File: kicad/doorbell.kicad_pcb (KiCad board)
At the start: 4 copper layers, 64 x 59 mm, 76 parts, among them J1 USB-C (USB4105), J2 WF26 bus, K1 GAQW212GS, K2 GAQY212GS, K3 GAQY412EH, K4 GAQY412EH, K5 G6K-2F-Y DC12, Q3 2N7002DW-7-F, SW1 BOOT, SW2 EN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

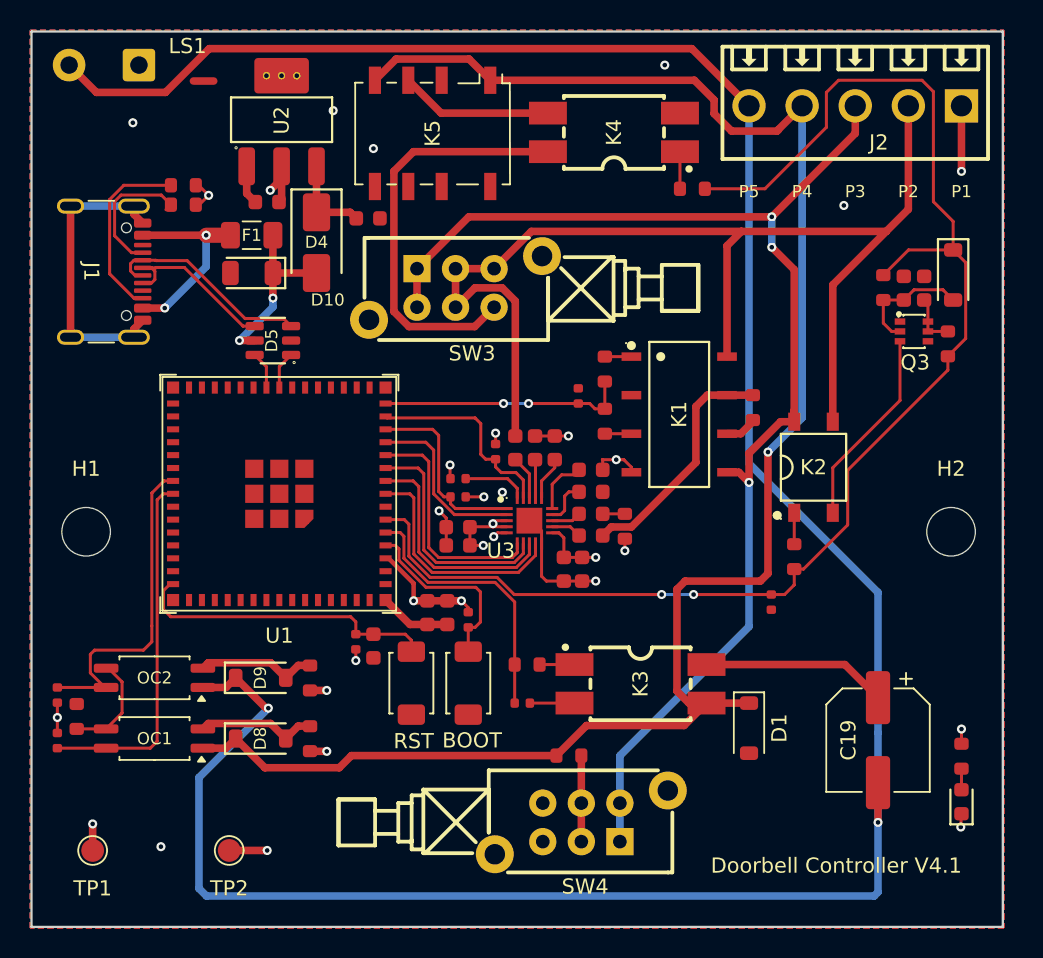
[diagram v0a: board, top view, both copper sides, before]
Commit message: PCB routing cleanup + K3 contact swap; confirm C1 polarity on the genuine WF26
Board (kicad/doorbell.*):
- P5 off the back layer: dropped the ~44 mm B.Cu bottom-edge run; OC2/D9 now tap
  P5 up the left edge to LS1, with C19 routed down the right edge. All-F.Cu, DRC clean.
- PTT_DRV all-F.Cu: removed the B.Cu hop under C16 (its via pair) by moving C16 up
  so PTT_DRV passes beneath it on the front; P2 now reaches C16 from the north, so
  the P2/PTT_DRV crossing that forced the hop is gone.
- Relocated the boot pull-downs to their MCU pins: R8 (DOOR_DRV) and R7 (PTT_DRV).
- K3 (chime mute): swapped the bidirectional PhotoMOS contact pins 3<->4
  (CHIME_C1 / P4) in the schematic for cleaner routing -- the output is symmetric.
- Zone refills; regenerated doorbell.pdf.

Docs:
- C1/C19 polarity bench-confirmed on the genuine WF26: + -> P4, - -> P5 (matches the
  wf26 reverse-engineered schematic and the V4 board; the old +->P5 assumption was the
  error). DESIGN.md + VERIFICATION.md updated, open item retired.
- reference/wf26.heic: genuine WF26 board photo (the polarity evidence).
- kicad/.gitignore: also ignore *_2d_view.png render artifacts.
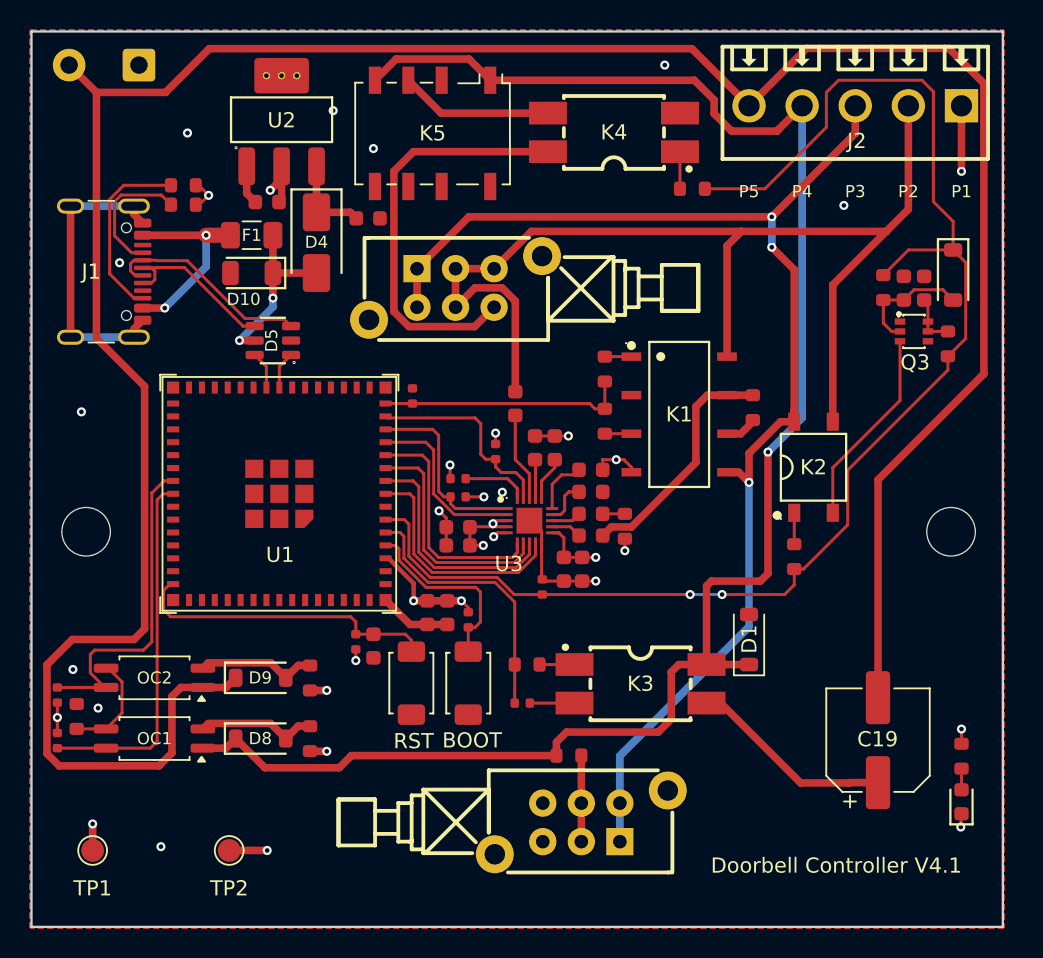
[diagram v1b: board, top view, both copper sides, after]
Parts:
- moved R8 15.1 mm to (50.1, 52.9), turned to 90 degrees
- moved R7 10.9 mm to (41.6, 40.3)
- moved D1 5.84 mm to (63.8, 56.4), turned to 90 degrees
- moved C16 2.92 mm to (48.4, 40.8)
- turned C19 to 90 degrees
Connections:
- K3 pad 3: /P4 -> /CHIME_C1
- K3 pad 4: /CHIME_C1 -> /P4
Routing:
- net /P5: track 169.8 -> 177.0 mm, vias 2 -> 0
- net /ES_MICP: track 2.91 -> 5.83 mm
- net /P2: track 77.2 -> 74.3 mm
- net /P4: track 118.0 -> 115.6 mm
- net GND: track 60.8 -> 59.4 mm, vias 20 -> 24
- net /CHIME_C1: track 12.2 -> 13.5 mm
- net /PTT_DRV: track 16.5 -> 16.4 mm, vias 2 -> 0

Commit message: Swap U1 to ESP32-C6-MINI-1U-H4: pinout, firmware, PCB re-layout
Replace the ESP32-S3-MINI-1U-N8 with the pin-compatible-in-spirit
ESP32-C6-MINI-1U-H4 (native USB-Serial-JTAG, u.FL external antenna,
4 MB flash) and carry the change through the whole stack.

- Schematic: U1 = ESP32-C6-MINI-1U-H4 with a new GPIO map (USB pads
  face north toward D5/J1, ES8311 I2S exits east in U3 pin order,
  I2C+MCLK off the NE corner). IO8 held high by R12 (SPI-boot strap,
  net IO8_STRAP); BOOT on IO9. U1 sourcing attrs set (LCSC C20627095,
  MPN, Value).
- Firmware: board esp32-c6-devkitc-1 / variant esp32c6 / flash 4MB;
  remap I2S/I2C/SSR-gate/opto-sense GPIOs to the C6 pinout.
  `esphome config` validates clean (only the expected GPIO4/GPIO5
  strapping-pin notices, which strap the unused SDIO boot edge).
- PCB: re-laid out for the C6 footprint and the new escape order.
- Docs: DESIGN.md MCU decision + GPIO-map rationale rewritten for the
  C6; VERIFICATION.md route-check note clarified.
- Component attrs: fill empty descriptions (J2, K1-K4, ...), replace
  library boilerplate with role descriptions, normalize resistor
  values (drop the inconsistent ohm suffix), fix R25 (6.8M one-shot).
- Tooling: build.sh gains a `sim` target; route.py float-sliver check
  now only fails islands actually wide enough to host a GND stitch via.
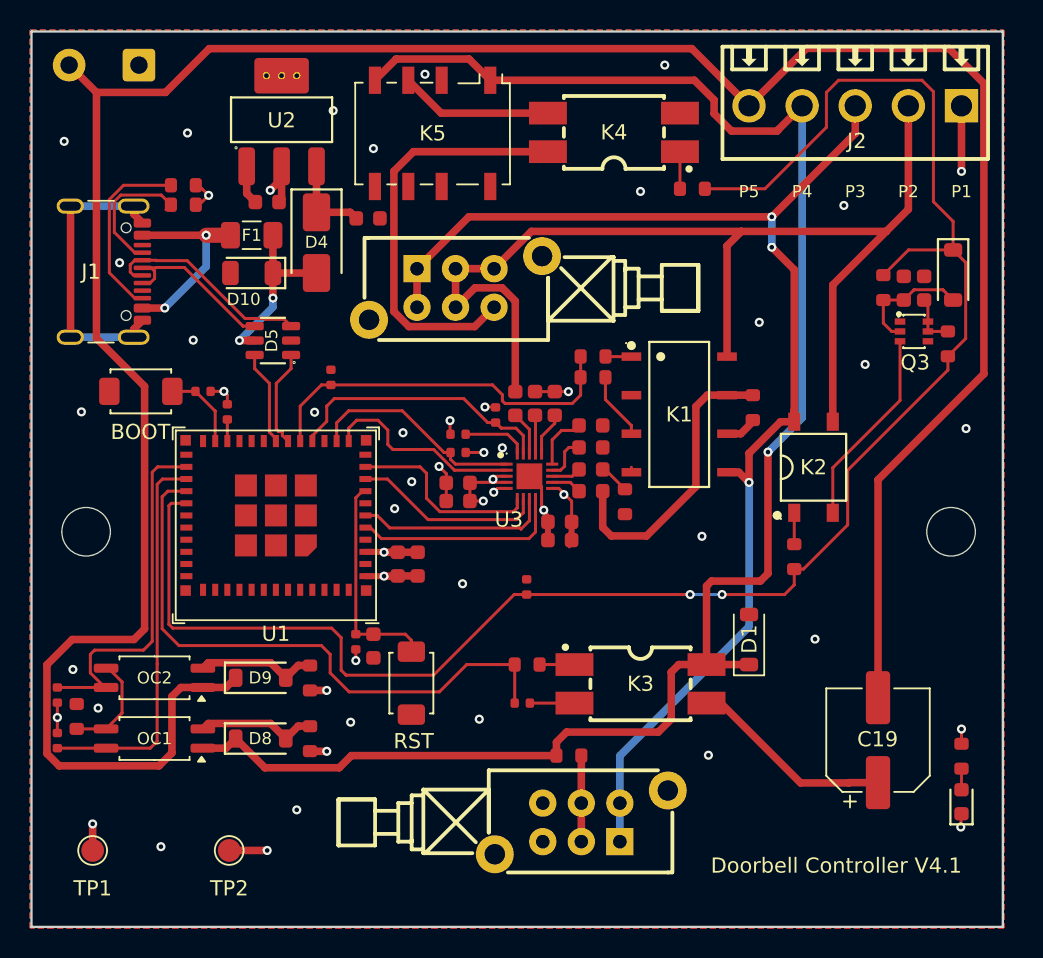
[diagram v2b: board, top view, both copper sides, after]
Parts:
- added R12: 10k, PCM_JLCPCB:R_0402, F.Cu at (29.4, 41.4)
- U1: value ESP32-S3-MINI-1U-N8 -> ESP32-C6-MINI-1U-H4; footprint PCM_Espressif:ESP32-S3-MINI-1U -> PCM_Espressif:ESP32-C6-MINI-1U
- moved SW1 28.9 mm to (23.7, 40.0), turned to 180 degrees
- moved R11 23.1 mm to (27.8, 40.0), turned to 180 degrees
- moved R7 5.51 mm to (36.2, 39.1)
- moved U1 4.13 mm to (32.6, 50.9)
- moved C3 3.75 mm to (41.9, 51.4)
- moved C6 3.75 mm to (40.6, 51.4)
- moved C9 3.13 mm to (51.3, 48.6), turned to 180 degrees
- moved R24 3.00 mm to (53.5, 39.1), turned to 180 degrees
- moved C11 2.93 mm to (53.3, 43.7)
- moved C12 2.93 mm to (51.0, 40.8)
- moved C13 2.93 mm to (53.3, 42.2)
- moved C14 2.93 mm to (53.3, 46.6)
- moved C17 2.93 mm to (49.6, 40.8)
- moved C7 2.93 mm to (44.6, 47.2)
- moved C8 2.93 mm to (44.6, 46.0)
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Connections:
- U1 pad 10: /I2S_DIN -> /I2S_BCLK
- U1 pad 11: /I2S_BCLK -> GND
- U1 pad 14: /I2C_SDA -> GND
- U1 pad 15: /PTT_DRV -> /I2C_SDA
- U1 pad 16: unconnected-(U1-IO12-Pad16) -> /PTT_DRV
- U1 pad 17: unconnected-(U1-IO13-Pad17) -> /USB_ESP_DN
- U1 pad 18: unconnected-(U1-IO14-Pad18) -> /USB_ESP_DP
- U1 pad 22: unconnected-(U1-IO18-Pad22) -> /IO8_STRAP
- U1 pad 23: /USB_ESP_DN -> /BOOT
- U1 pad 24: /USB_ESP_DP -> unconnected-(U1-GPIO18-Pad24)
- U1 pad 26: unconnected-(U1-IO26-Pad26) -> /OC2_OUT
- U1 pad 27: unconnected-(U1-IO47-Pad27) -> /OC1_OUT
- U1 pad 28: unconnected-(U1-IO33-Pad28) -> /MUTE_DRV
- U1 pad 29: unconnected-(U1-IO34-Pad29) -> /DOOR_DRV
- U1 pad 36: unconnected-(U1-IO40-Pad36) -> GND
- U1 pad 37: /OC2_OUT -> GND
- U1 pad 38: /OC1_OUT -> GND
- U1 pad 39: unconnected-(U1-TXD0-Pad39) -> GND
- U1 pad 4: /BOOT -> unconnected-(U1-NC-Pad4)
- U1 pad 40: unconnected-(U1-RXD0-Pad40) -> GND
- U1 pad 41: unconnected-(U1-IO45-Pad41) -> GND
- U1 pad 44: unconnected-(U1-IO46-Pad44) -> GND
- U1 pad 45: /EN -> GND
- U1 pad 5: /MUTE_DRV -> /I2S_DOUT
- U1 pad 6: /DOOR_DRV -> /I2S_WS
- U1 pad 8: /I2S_DOUT -> /EN
- U1 pad 9: /I2S_WS -> /I2S_DIN
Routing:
- net /DOOR_DRV: track 93.9 -> 118.7 mm
- net /MUTE_DRV: track 18.2 -> 39.6 mm
- net /PTT_DRV: track 16.4 -> 24.9 mm
- net GND: track 59.4 -> 51.0 mm, vias 24 -> 41
- net /BOOT: track 12.5 -> 5.34 mm
- net /EN: track 20.4 -> 14.4 mm
- net /I2C_SDA: track 13.5 -> 18.0 mm
- net /USB_ESP_DN: track 2.47 -> 6.55 mm
- net /USB_ESP_DP: track 2.47 -> 6.25 mm
- net /TALK_BRIDGE: track 15.9 -> 19.4 mm
- net /ES_MICP: track 5.83 -> 2.91 mm
- net /I2S_DIN: track 15.5 -> 12.6 mm
- net /K1_LED_B: track 1.75 -> 4.42 mm
- net /I2S_BCLK: track 15.5 -> 12.9 mm
- net /I2S_WS: track 15.5 -> 12.8 mm
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
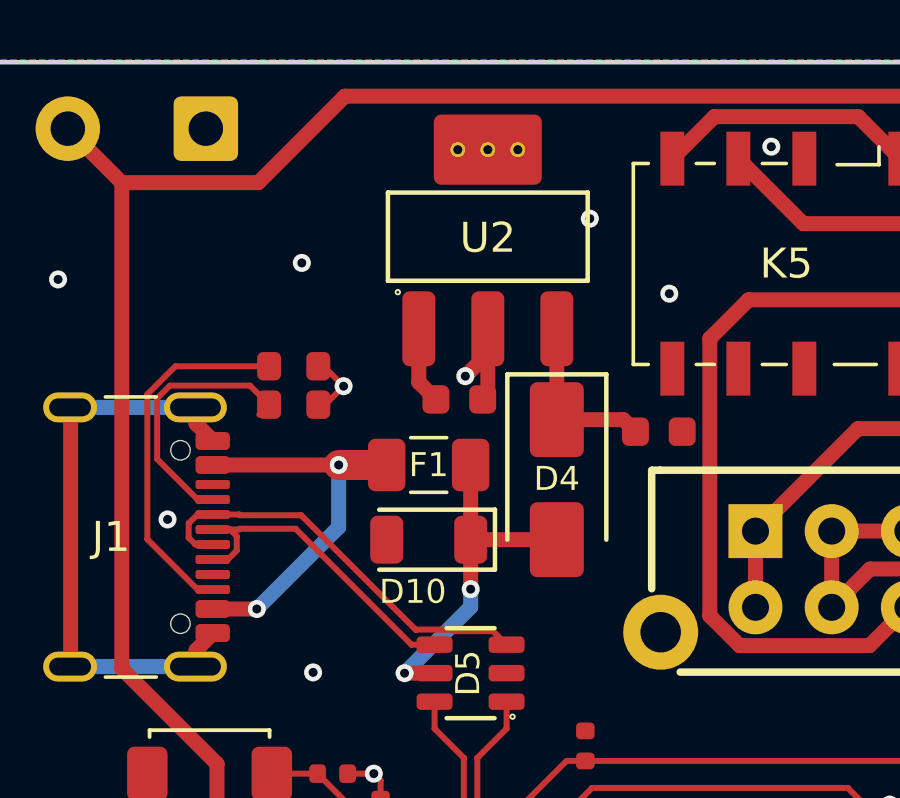
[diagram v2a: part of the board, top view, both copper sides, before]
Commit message: Door watchdog: R25/C20 → 3 MΩ / 2.2 µF for leakage margin (both free)
Keep the ~6.7 s door-release one-shot timing (the validated 6.8 MΩ·1 µF
band) but trade R down / C up: R25 6.8 MΩ→3 MΩ (C23213 Extended →
C23156 Preferred) and C20 1 µF→2.2 µF 16 V (C15849 → C23630 Basic).
The lower gate-node impedance draws ~2.3× more current at threshold,
cutting the leakage / "never-releases" risk on this high-MΩ node — the
failure direction that matters for DOOR-5 — and both parts are now free,
dropping one Extended setup fee. sim/test confirms ~6.68 s release; the
fast corner (~2.4 s, ≈2.0 s with the 16 V cap's bias derating) still
clears the 1.75 s firmware door pulse, so a normal open is never cut
short. (5.1 MΩ was rejected: its ~1.84 s min-Vgs(th) corner sat too
close to the pulse.)

Also fixes stale part metadata found along the way:
- R25's cached fields claimed 6.8 kΩ / Basic while LCSC was the 6.8 MΩ
  Extended part — corrected to match.
- C20's description was a wrong "EN reset RC" copy-paste; it's the
  watchdog timing cap.

Docs: DESIGN.md watchdog timing + the R-down/C-up leakage rationale;
JLCPCB-BASIC-PARTS.md reclassification (R25 → Preferred-free, C20 → new
Basic line; 15 Basic + 2 Preferred / 31 distinct, 14 Extended ≈ $42)
plus the C6/U1 BOM refresh (U1 → C20627095, R12 into the 10 k group);
sim/test watchdog comments.
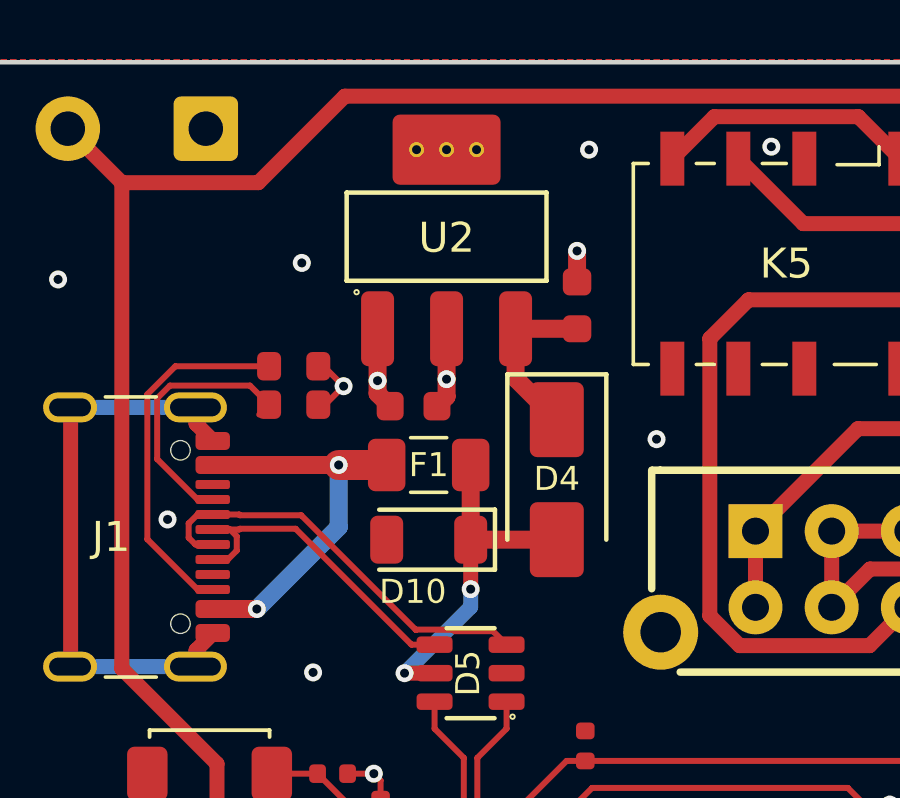
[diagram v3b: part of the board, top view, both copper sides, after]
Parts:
- C20: value 1uF -> 2.2uF
- R16: value 2.2kΩ -> 2.2k
- R17: value 22kΩ -> 22k
- R25: value 6.8MΩ -> 3M
- moved C2 5.01 mm to (35.9, 24.4), turned to 90 degrees
- moved C4 1.54 mm to (30.5, 27.8)
- moved U2 1.38 mm to (31.6, 22.2)
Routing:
- net GND: track 51.0 -> 52.2 mm, vias 41 -> 43
- net +3V3: track 28.4 -> 27.7 mm
